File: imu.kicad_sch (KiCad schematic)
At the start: 11 parts, among them U402 BNO055, X401 Q13FC1350000400

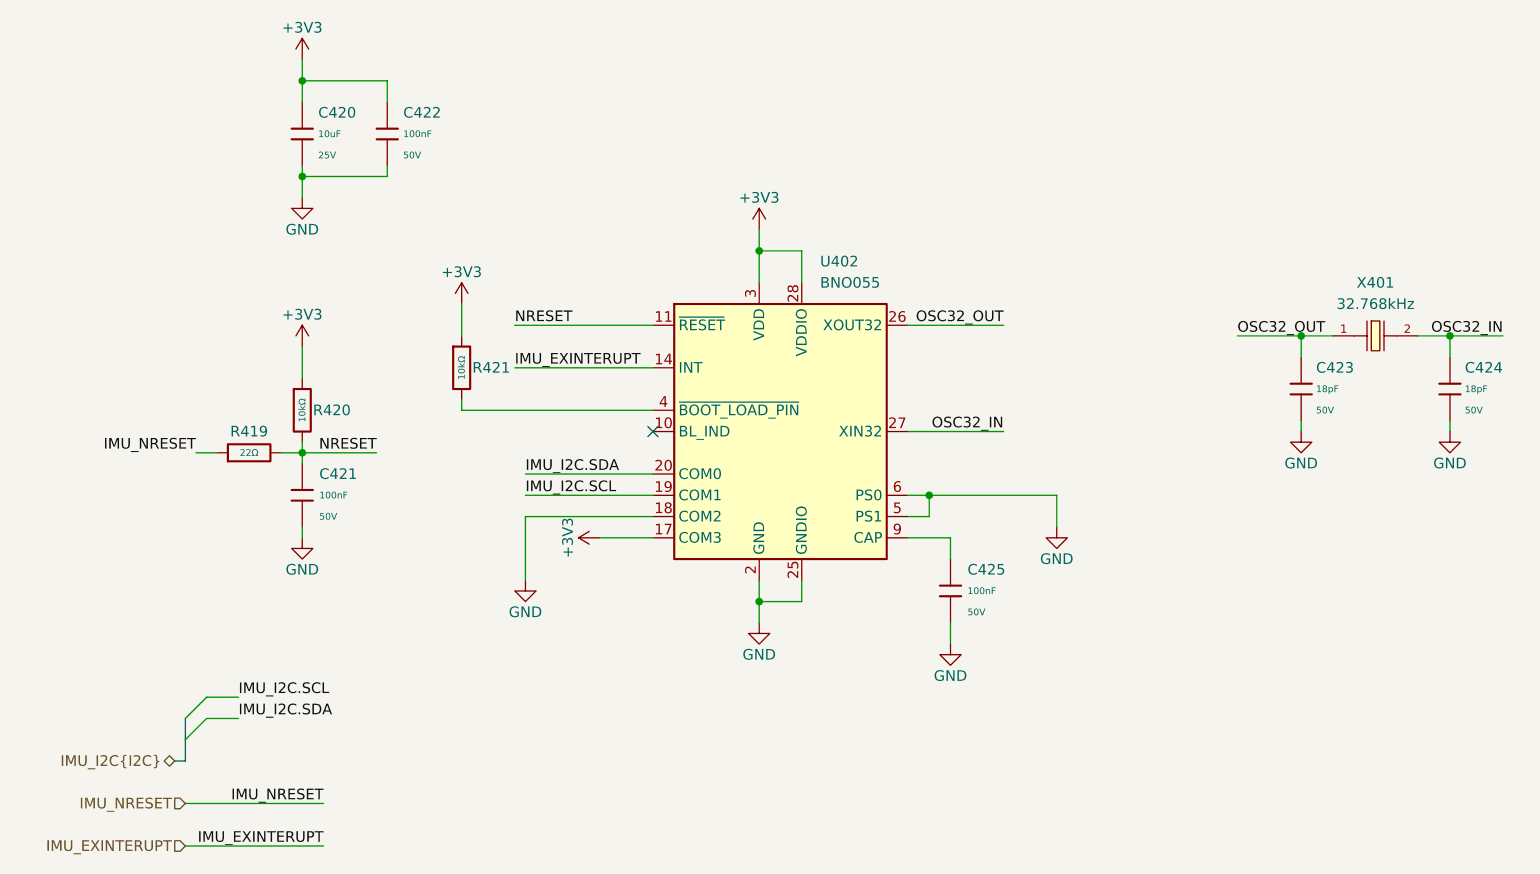
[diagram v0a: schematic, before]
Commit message: final check , added pull up resistors on i2c
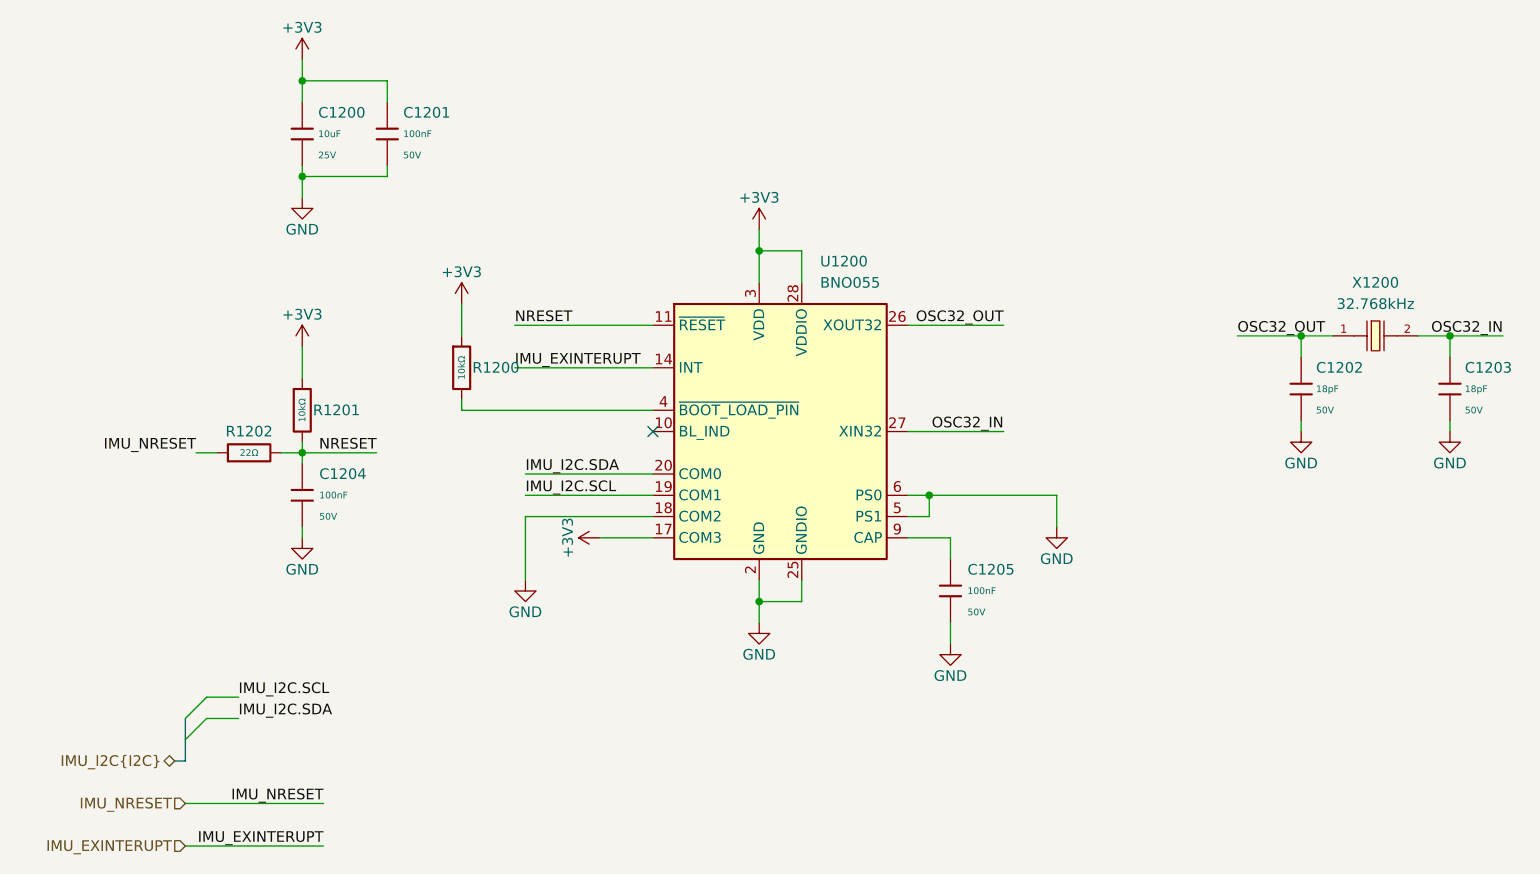
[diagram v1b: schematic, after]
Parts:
- renumbered C420 to C1200, C422 to C1201, C423 to C1202, C424 to C1203, C421 to C1204, C425 to C1205, R421 to R1200, R420 to R1201, R419 to R1202, U402 to U1200, X401 to X1200
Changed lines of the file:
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@@
 	(title_block
 		(title "ModuCard nav module")
+		(rev "1.0")
 		(comment 2 "Project author: Patryk Dudziński")
 	)
@@
 	(label "OSC32_IN"
 		(at 142.24 69.85 180)
+		(fields_autoplaced yes)
 		(effects
 			(font
@@
 	(label "IMU_I2C.SDA"
 		(at 85.09 74.93 0)
+		(fields_autoplaced yes)
 		(effects
 			(font
@@
 	(label "IMU_EXINTERUPT"
 		(at 60.96 119.38 180)
+		(fields_autoplaced yes)
 		(effects
 			(font
@@
 	(label "NRESET"
 		(at 67.31 72.39 180)
+		(fields_autoplaced yes)
 		(effects
 			(font
@@
 	(label "OSC32_OUT"
 		(at 142.24 57.15 180)
+		(fields_autoplaced yes)
 		(effects
 			(font
@@
 	(label "IMU_I2C.SDA"
 		(at 50.8 104.14 0)
+		(fields_autoplaced yes)
 		(effects
 			(font
@@
 	(label "OSC32_IN"
 		(at 201.93 58.42 180)
+		(fields_autoplaced yes)
 		(effects
 			(font
@@
 	(label "NRESET"
 		(at 83.82 57.15 0)
+		(fields_autoplaced yes)
 		(effects
 			(font
@@
 	(label "IMU_I2C.SCL"
 		(at 50.8 101.6 0)
+		(fields_autoplaced yes)
 		(effects
 			(font
@@
 	(label "IMU_NRESET"
 		(at 45.72 72.39 180)
+		(fields_autoplaced yes)
 		(effects
 			(font
@@
 	(label "IMU_EXINTERUPT"
 		(at 83.82 62.23 0)
+		(fields_autoplaced yes)
 		(effects
 			(font
@@
 	(label "IMU_NRESET"
 		(at 60.96 114.3 180)
+		(fields_autoplaced yes)
 		(effects
 			(font
@@
 	(label "OSC32_OUT"
 		(at 170.18 58.42 0)
+		(fields_autoplaced yes)
 		(effects
 			(font
@@
 	(label "IMU_I2C.SCL"
 		(at 85.09 77.47 0)
+		(fields_autoplaced yes)
 		(effects
 			(font
@@
 		(shape input)
 		(at 44.45 119.38 180)
+		(fields_autoplaced yes)
 		(effects
 			(font
@@
 		(shape bidirectional)
 		(at 43.18 109.22 180)
+		(fields_autoplaced yes)
 		(effects
 			(font
@@
 		(shape input)
 		(at 44.45 114.3 180)
+		(fields_autoplaced yes)
 		(effects
 			(font
@@
 		(on_board yes)
 		(dnp no)
-		(property "Reference" "#PWR0445"
+		(property "Reference" "#PWR01200"
 			(at 58.42 29.21 0)
 			(effects
@@
 			(project "nav-module"
 				(path "/090a8e41-87a8-4fb1-998b-60a2c0dc4cee/89e62ca8-6649-452b-b3fd-35dd46316796"
-					(reference "#PWR0445")
+					(reference "#PWR01200")
 					(unit 1)
 				)
@@
 		(on_board yes)
 		(dnp no)
-		(property "Reference" "C424"
+		(property "Reference" "C1203"
 			(at 197.358 62.2299 0)
 			(effects
@@
 			(project "nav-module"
 				(path "/090a8e41-87a8-4fb1-998b-60a2c0dc4cee/89e62ca8-6649-452b-b3fd-35dd46316796"
-					(reference "C424")
+					(reference "C1203")
 					(unit 1)
 				)
@@
 		(on_board yes)
 		(dnp no)
-		(property "Reference" "#PWR0451"
+		(property "Reference" "#PWR01207"
 			(at 148.59 87.63 0)
 			(effects
@@
 			(project "nav-module"
 				(path "/090a8e41-87a8-4fb1-998b-60a2c0dc4cee/89e62ca8-6649-452b-b3fd-35dd46316796"
-					(reference "#PWR0451")
+					(reference "#PWR01207")
 					(unit 1)
 				)
@@
 		(on_board yes)
 		(dnp no)
-		(property "Reference" "R420"
+		(property "Reference" "R1201"
 			(at 59.69 67.31 0)
 			(effects
@@
 			(project "nav-module"
 				(path "/090a8e41-87a8-4fb1-998b-60a2c0dc4cee/89e62ca8-6649-452b-b3fd-35dd46316796"
-					(reference "R420")
+					(reference "R1201")
 					(unit 1)
 				)
@@
 		(on_board yes)
 		(dnp no)
-		(property "Reference" "C423"
+		(property "Reference" "C1202"
 			(at 179.578 62.23 0)
 			(effects
@@
 			(project "nav-module"
 				(path "/090a8e41-87a8-4fb1-998b-60a2c0dc4cee/89e62ca8-6649-452b-b3fd-35dd46316796"
-					(reference "C423")
+					(reference "C1202")
 					(unit 1)
 				)
@@
 		(on_board yes)
 		(dnp no)
-		(property "Reference" "R419"
+		(property "Reference" "R1202"
 			(at 52.07 69.85 90)
 			(effects
@@
 			(project "nav-module"
 				(path "/090a8e41-87a8-4fb1-998b-60a2c0dc4cee/89e62ca8-6649-452b-b3fd-35dd46316796"
-					(reference "R419")
+					(reference "R1202")
 					(unit 1)
 				)
@@
 		(on_board yes)
 		(dnp no)
-		(property "Reference" "#PWR0447"
+		(property "Reference" "#PWR01204"
 			(at 58.42 63.5 0)
 			(effects
@@
 			(project "nav-module"
 				(path "/090a8e41-87a8-4fb1-998b-60a2c0dc4cee/89e62ca8-6649-452b-b3fd-35dd46316796"
-					(reference "#PWR0447")
+					(reference "#PWR01204")
 					(unit 1)
 				)
@@
 		(on_board yes)
 		(dnp no)
-		(property "Reference" "C420"
+		(property "Reference" "C1200"
 			(at 60.325 31.75 0)
 			(effects
@@
 			(project "nav-module"
 				(path "/090a8e41-87a8-4fb1-998b-60a2c0dc4cee/89e62ca8-6649-452b-b3fd-35dd46316796"
-					(reference "C420")
+					(reference "C1200")
 					(unit 1)
 				)
@@
 		(on_board yes)
 		(dnp no)
-		(property "Reference" "#PWR0450"
+		(property "Reference" "#PWR01206"
 			(at 195.58 76.2 0)
 			(effects
@@
 			(project "nav-module"
 				(path "/090a8e41-87a8-4fb1-998b-60a2c0dc4cee/89e62ca8-6649-452b-b3fd-35dd46316796"
-					(reference "#PWR0450")
+					(reference "#PWR01206")
 					(unit 1)
 				)
@@
 		(dnp no)
 		(fields_autoplaced yes)
-		(property "Reference" "U402"
+		(property "Reference" "U1200"
 			(at 120.3041 49.53 0)
 			(effects
@@
 			(project ""
 				(path "/090a8e41-87a8-4fb1-998b-60a2c0dc4cee/89e62ca8-6649-452b-b3fd-35dd46316796"
-					(reference "U402")
+					(reference "U1200")
 					(unit 1)
 				)
@@
 		(on_board yes)
 		(dnp no)
-		(property "Reference" "#PWR0449"
+		(property "Reference" "#PWR01205"
 			(at 177.8 76.2 0)
 			(effects
@@
 			(project "nav-module"
 				(path "/090a8e41-87a8-4fb1-998b-60a2c0dc4cee/89e62ca8-6649-452b-b3fd-35dd46316796"
-					(reference "#PWR0449")
+					(reference "#PWR01205")
 					(unit 1)
 				)
@@
 		(on_board yes)
 		(dnp no)
-		(property "Reference" "#PWR0446"
+		(property "Reference" "#PWR01201"
 			(at 58.42 48.26 0)
 			(effects
@@
 			(project "nav-module"
 				(path "/090a8e41-87a8-4fb1-998b-60a2c0dc4cee/89e62ca8-6649-452b-b3fd-35dd46316796"
-					(reference "#PWR0446")
+					(reference "#PWR01201")
 					(unit 1)
 				)
@@
 		(on_board yes)
 		(dnp no)
-		(property "Reference" "#PWR0456"
+		(property "Reference" "#PWR01203"
 			(at 77.47 58.42 0)
 			(effects
@@
 			(project "nav-module"
 				(path "/090a8e41-87a8-4fb1-998b-60a2c0dc4cee/89e62ca8-6649-452b-b3fd-35dd46316796"
-					(reference "#PWR0456")
+					(reference "#PWR01203")
 					(unit 1)
 				)
@@
 		(on_board yes)
 		(dnp no)
-		(property "Reference" "C421"
+		(property "Reference" "C1204"
 			(at 60.452 74.93 0)
 			(effects
@@
 			(project "nav-module"
 				(path "/090a8e41-87a8-4fb1-998b-60a2c0dc4cee/89e62ca8-6649-452b-b3fd-35dd46316796"
-					(reference "C421")
+					(reference "C1204")
 					(unit 1)
 				)
@@
 		(on_board yes)
 		(dnp no)
-		(property "Reference" "#PWR0457"
+		(property "Reference" "#PWR01209"
 			(at 97.79 82.55 0)
 			(effects
@@
 			(project "nav-module"
 				(path "/090a8e41-87a8-4fb1-998b-60a2c0dc4cee/89e62ca8-6649-452b-b3fd-35dd46316796"
-					(reference "#PWR0457")
+					(reference "#PWR01209")
 					(unit 1)
 				)
@@
 		(on_board yes)
 		(dnp no)
-		(property "Reference" "#PWR0448"
+		(property "Reference" "#PWR01208"
 			(at 58.42 88.9 0)
 			(effects
@@
 			(project "nav-module"
 				(path "/090a8e41-87a8-4fb1-998b-60a2c0dc4cee/89e62ca8-6649-452b-b3fd-35dd46316796"
-					(reference "#PWR0448")
+					(reference "#PWR01208")
 					(unit 1)
 				)
@@
 		(on_board yes)
 		(dnp no)
-		(property "Reference" "C422"
+		(property "Reference" "C1201"
 			(at 70.485 31.7499 0)
 			(effects
@@
 			(project "nav-module"
 				(path "/090a8e41-87a8-4fb1-998b-60a2c0dc4cee/89e62ca8-6649-452b-b3fd-35dd46316796"
-					(reference "C422")
+					(reference "C1201")
 					(unit 1)
 				)
@@
 		(on_board yes)
 		(dnp no)
-		(property "Reference" "#PWR0453"
+		(property "Reference" "#PWR01211"
 			(at 113.03 99.06 0)
 			(effects
@@
 			(project "nav-module"
 				(path "/090a8e41-87a8-4fb1-998b-60a2c0dc4cee/89e62ca8-6649-452b-b3fd-35dd46316796"
-					(reference "#PWR0453")
+					(reference "#PWR01211")
 					(unit 1)
 				)
@@
 		(on_board yes)
 		(dnp no)
-		(property "Reference" "C425"
+		(property "Reference" "C1205"
 			(at 137.922 86.36 0)
 			(effects
@@
 			(project "nav-module"
 				(path "/090a8e41-87a8-4fb1-998b-60a2c0dc4cee/89e62ca8-6649-452b-b3fd-35dd46316796"
-					(reference "C425")
+					(reference "C1205")
 					(unit 1)
 				)
@@
 		(dnp no)
 		(fields_autoplaced yes)
-		(property "Reference" "X401"
+		(property "Reference" "X1200"
 			(at 186.69 52.07 0)
 			(effects
@@
 			(project "nav-module"
 				(path "/090a8e41-87a8-4fb1-998b-60a2c0dc4cee/89e62ca8-6649-452b-b3fd-35dd46316796"
-					(reference "X401")
+					(reference "X1200")
 					(unit 1)
 				)
@@
 		(on_board yes)
 		(dnp no)
-		(property "Reference" "R421"
+		(property "Reference" "R1200"
 			(at 78.74 62.23 0)
 			(effects
@@
 			(project "nav-module"
 				(path "/090a8e41-87a8-4fb1-998b-60a2c0dc4cee/89e62ca8-6649-452b-b3fd-35dd46316796"
-					(reference "R421")
+					(reference "R1200")
 					(unit 1)
 				)
@@
 		(on_board yes)
 		(dnp no)
-		(property "Reference" "#PWR0452"
+		(property "Reference" "#PWR01212"
 			(at 135.89 101.6 0)
 			(effects
@@
 			(project "nav-module"
 				(path "/090a8e41-87a8-4fb1-998b-60a2c0dc4cee/89e62ca8-6649-452b-b3fd-35dd46316796"
-					(reference "#PWR0452")
+					(reference "#PWR01212")
 					(unit 1)
 				)
@@
 		(on_board yes)
 		(dnp no)
-		(property "Reference" "#PWR0455"
+		(property "Reference" "#PWR01210"
 			(at 85.09 93.98 0)
 			(effects
@@
 			(project "nav-module"
 				(path "/090a8e41-87a8-4fb1-998b-60a2c0dc4cee/89e62ca8-6649-452b-b3fd-35dd46316796"
-					(reference "#PWR0455")
+					(reference "#PWR01210")
 					(unit 1)
 				)
@@
 		(on_board yes)
 		(dnp no)
-		(property "Reference" "#PWR0454"
+		(property "Reference" "#PWR01202"
 			(at 113.03 49.53 0)
 			(effects
@@
 			(project "nav-module"
 				(path "/090a8e41-87a8-4fb1-998b-60a2c0dc4cee/89e62ca8-6649-452b-b3fd-35dd46316796"
-					(reference "#PWR0454")
+					(reference "#PWR01202")
 					(unit 1)
 				)
